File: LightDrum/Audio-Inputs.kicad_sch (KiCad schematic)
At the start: 18 parts, among them J4 XLR3, J5 SJ-43515RS-SMT-TR, K3 2-SW-RELAY, U41 SSM3K361R_SOT23F, U7 OPA1652

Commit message: Add docs and gerbers for REV7
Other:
- title: Audio Inputs -> LightDrum
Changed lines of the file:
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@@
   (paper "A4")
   (title_block
-    (title "Audio Inputs")
-    (rev "REV6")
+    (title "LightDrum")
+    (rev "REV7")
     (company "Daxxn Industries")
   )

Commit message: First pass over schematic (WIP)
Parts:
- removed K3: 2-SW-RELAY, Daxxn_Relays:AGQ200S4HZ, symbol Daxxn_Relays:2-SW-RELAY
- removed R100, R99: ${DIFF-RES}, Resistor_SMD:R_0805_2012Metric, symbol Device:R_Small_US
- removed R101: 470${RES}, Resistor_SMD:R_0805_2012Metric, symbol Device:R_Small_US
- removed R102: 100${RES}, Resistor_SMD:R_0805_2012Metric, symbol Device:R_Small_US
- removed R103: ${P-RES}, Resistor_SMD:R_0805_2012Metric, symbol Device:R_Small_US
- removed U41: SSM3K361R_SOT23F, Package_TO_SOT_SMD:SOT-23, symbol Daxxn_Transistors:SSM3K361R_SOT23F
- removed U7: OPA1652, Package_SO:VSSOP-8_3.0x3.0mm_P0.65mm, symbol Daxxn_OPAMP:OPA1652
- added C12, C16: 100nF, Capacitor_SMD:C_0603_1608Metric, symbol Device:C_Small
- added C13, C14, C17, C18: 10uF, Capacitor_SMD:C_1210_3225Metric, symbol Device:C_Small
- added C15, C19: 4.7uF, Capacitor_SMD:C_0805_2012Metric, symbol Device:C_Small
- added R10, R11: 330, Resistor_SMD:R_0805_2012Metric, symbol Device:R_Small_US
- added R4, R7: 14.67K, Resistor_SMD:R_0603_1608Metric, symbol Device:R_Small_US
- added R5, R8: 10K, Resistor_SMD:R_0603_1608Metric, symbol Device:R_Small_US
- added R6, R9: 100K, Resistor_SMD:R_0603_1608Metric, symbol Device:R_Small_US
- added RV1, RV2: 30K, Potentiometer_SMD:Potentiometer_Bourns_TC33X_Vertical, symbol Device:R_Potentiometer_Small
- added U-HP-VREF1, U-XLR-VREF1: TPS7A94, Daxxn_Packages:WSON-10-1EP_3x3mm, symbol Daxxn_Regulators:TPS7A94
- added U-HP1, U-XLR1: MCP3550-60-ESN, symbol Analog_ADC:MCP3550-60-ESN
- D8: value HP IND - RED -> HP IND - BLUE
- D9: value XLR IND - RED -> XLR IND - BLUE
- R92, R97, R98: value 100${RES} -> 100
- R93: value ${P-RES} -> 10K
- R95, R96: value ${DIFF-RES} -> 100
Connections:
- net GND: now also J4.1, C12.2, C13.2, C14.2, C15.2, C16.2, C17.2, C18.2, C19.2, R6.2, R9.2, RV1.2, RV1.3, RV2.2, RV2.3, U-HP-VREF1.11 (GND), U-HP-VREF1.6 (GND), U-HP1.4 (VSS), U-XLR-VREF1.11 (GND), U-XLR-VREF1.6 (GND), U-XLR1.4 (VSS)
- net at R97.2, R98.2: now also U-HP1.2 (Vin+)
- net at R96.2: now also U-XLR1.3 (Vin-)
- net at R95.2: now also U-XLR1.2 (Vin+)
- net at D9.2 (A): now also R11.2
- net at D8.2 (A): now also R10.2
- net GNDA: no longer names the net of J5.S
- net GNDA: now also U-HP1.3 (Vin-); no longer J4.1
- new net: R5.2, U-XLR-VREF1.3 (EN_UV)
- new net: R4.2, R6.1, U-XLR-VREF1.5 (FB_PG)
- new net: C15.1, RV1.1, U-XLR-VREF1.7 (NR/SS)
- new net: R7.2, R9.1, U-HP-VREF1.5 (FB_PG)
- new net: R8.2, U-HP-VREF1.3 (EN_UV)
- new net: C19.1, RV2.1, U-HP-VREF1.7 (NR/SS)
- new net HP-ADC-CS: U-HP1.7 (~{CS})
- new net HP-SEL-IND: R10.1
- new net HP-VREF: C17.1, R7.1, U-HP-VREF1.10 (OUT), U-HP-VREF1.8 (SNS), U-HP-VREF1.9 (OUT), U-HP1.1 (Vref)
- new net HP-VREF-PG: U-HP-VREF1.4 (PG)
- new net SPI-COPI: U-HP1.6 (SDO/~{RDY}), U-XLR1.6 (SDO/~{RDY})
- new net SPI-SCLK: U-HP1.5 (SCK), U-XLR1.5 (SCK)
- new net VDD: C12.1, C14.1, C16.1, C18.1, R5.1, R8.1, U-HP-VREF1.1 (IN), U-HP-VREF1.2 (IN), U-HP1.8 (VDD), U-XLR-VREF1.1 (IN), U-XLR-VREF1.2 (IN), U-XLR1.8 (VDD)
- new net XLR-ADC-CS: U-XLR1.7 (~{CS})
- new net XLR-SEL-IND: R11.1
- new net XLR-VREF: C13.1, R4.1, U-XLR-VREF1.10 (OUT), U-XLR-VREF1.8 (SNS), U-XLR-VREF1.9 (OUT), U-XLR1.1 (Vref)
- new net XLR-VREF-PG: U-XLR-VREF1.4 (PG)
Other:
- note added: "AUDIO ADCS"
- note added: "Extra adjustable regulation on the ADCs VREF lines."
- note added: "THIS IS OVERKILL AS FUCK. I LIKE IT."
- note added: "The HP-SWITCH sends a signal to the MC, setting the HP jack as a possible audio source."
- note removed: "AUDIO SOURCE SELECTION"
- moved on the sheet: D8, D9, J4, J5, R92, R93, R95, R96, R97, R98

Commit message: Clean up and remove old files
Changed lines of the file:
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@@
     (stroke (width 0) (type default) (color 0 0 0 0))
   )
-  (wire (pts (xy 134.62 38.1) (xy 138.43 38.1))
+  (wire (pts (xy 123.19 38.1) (xy 138.43 38.1))
     (stroke (width 0) (type default) (color 0 0 0 0))
   )
@@
     (effects (font (size 1.27 1.27)) (justify left bottom))
   )
+  (label "XLR-VREF" (at 123.19 38.1 0)
+    (effects (font (size 1.27 1.27)) (justify left bottom))
+  )
   (label "XLR-VREF" (at 69.85 63.5 0)
     (effects (font (size 1.27 1.27)) (justify left bottom))
@@
     (effects (font (size 1.27 1.27)) (justify right))
   )
-  (hierarchical_label "XLR-VREF" (shape output) (at 134.62 38.1 180)
-    (effects (font (size 1.27 1.27)) (justify right))
-  )

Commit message: General component placement
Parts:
- removed U-HP1, U-XLR1: MCP3550-60-ESN, symbol Analog_ADC:MCP3550-60-ESN
- added U-HP201, U-XLR201: MCP3553-ESN, Package_SO:MSOP-8_3x3mm_P0.65mm, symbol Analog_ADC:MCP3553-ESN
- J202: renamed from J5; PartNumber (none) -> 0407-0001
- R202: renamed from R5; footprint Resistor_SMD:R_0603_1608Metric -> Resistor_SMD:R_0402_1005Metric
- R208: renamed from R8; footprint Resistor_SMD:R_0603_1608Metric -> Resistor_SMD:R_0402_1005Metric
- RV201: renamed from RV1; footprint Potentiometer_SMD:Potentiometer_Bourns_TC33X_Vertical -> Daxxn_Switches:Bourns_TC33X
- RV202: renamed from RV2; footprint Potentiometer_SMD:Potentiometer_Bourns_TC33X_Vertical -> Daxxn_Switches:Bourns_TC33X
- renumbered C12 to C201, C13 to C202, C14 to C203, C15 to C204, C16 to C205, C17 to C206, C18 to C207, C19 to C208, D8 to D201, D9 to D202, J4 to J201, R4 to R201, R95 to R203, R96 to R204, R6 to R205, R97 to R206, R7 to R207, R98 to R209, R9 to R210, R92 to R211, R93 to R212, R10 to R213, R11 to R214, U-HP-VREF1 to U-HP-VREF201, U-XLR-VREF1 to U-XLR-VREF201
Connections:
- net GND: now also U-HP201.4 (VSS), U-XLR201.4 (VSS)
- net HP-ADC-CS: now also U-HP201.7 (~{CS})
- net HP-VREF: now also U-HP201.1 (Vref)
- net SPI-COPI: now also U-HP201.6 (SDO/~{RDY}), U-XLR201.6 (SDO/~{RDY})
- net SPI-SCLK: now also U-HP201.5 (SCK), U-XLR201.5 (SCK)
- net VDD: now also U-HP201.8 (VDD), U-XLR201.8 (VDD)
- net XLR-ADC-CS: now also U-XLR201.7 (~{CS})
- net XLR-VREF: now also U-XLR201.1 (Vref)
- net HP+: now reaches R206.2, R209.2
- net HP+: now also U-HP201.2 (Vin+)
- net XLR-: now reaches R204.2
- net XLR-: now also U-XLR201.3 (Vin-)
- net XLR+: now reaches R203.2
- net XLR+: now also U-XLR201.2 (Vin+)
- net HP-: now reaches J202.S
- net HP-: now also U-HP201.3 (Vin-)

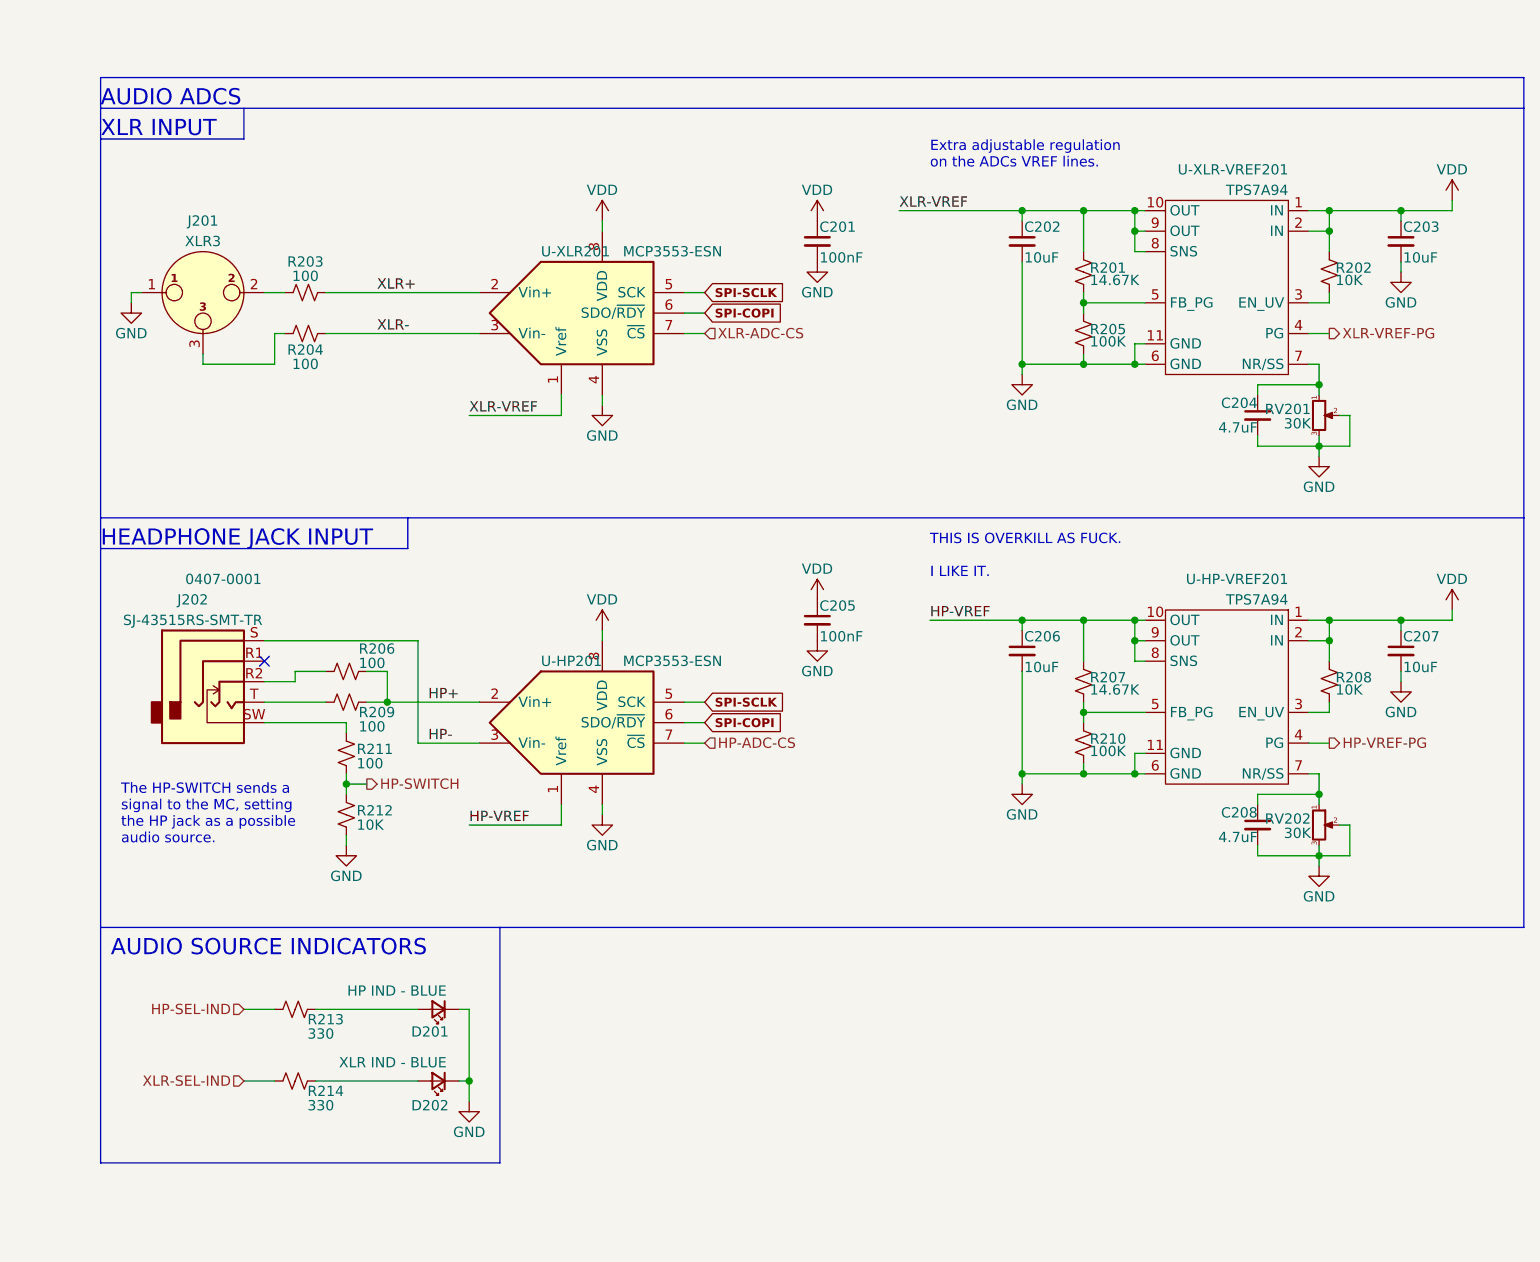
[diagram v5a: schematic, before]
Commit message: Simplify analog power supply and add some routing
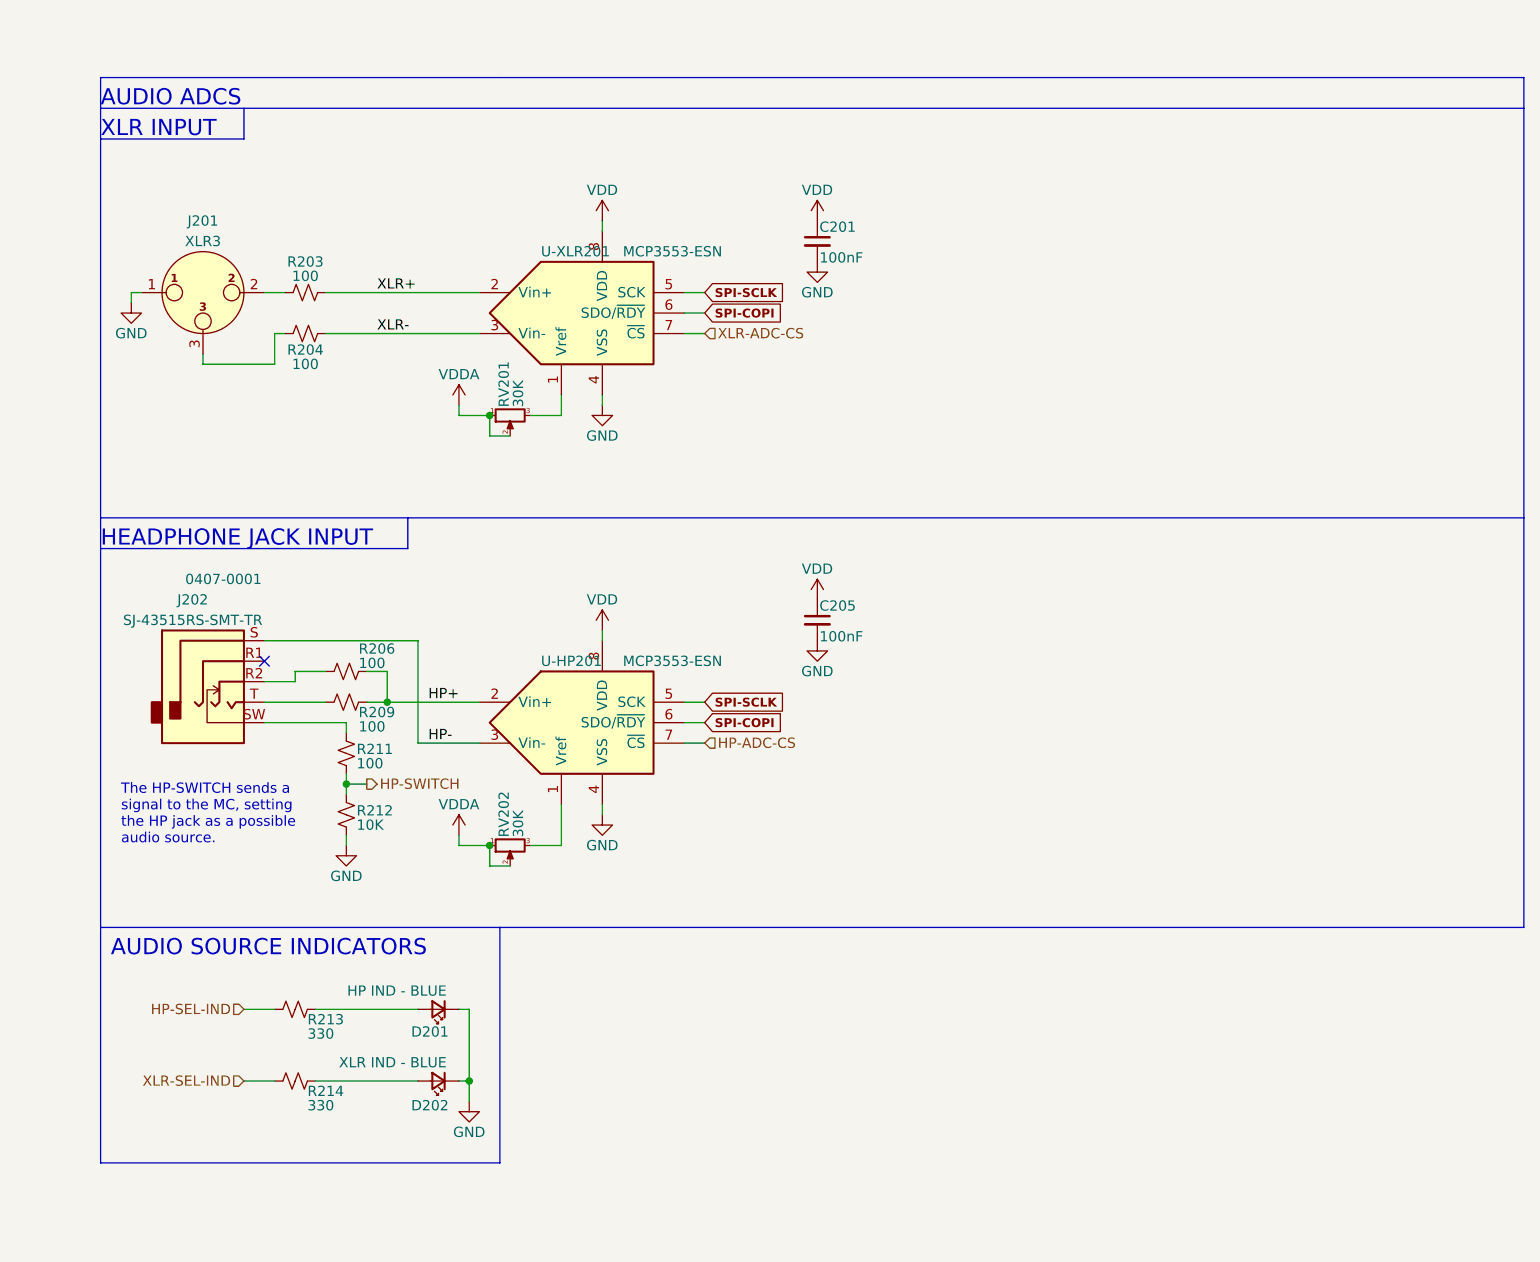
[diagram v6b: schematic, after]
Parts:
- removed C202, C203, C206, C207: 10uF, Capacitor_SMD:C_1210_3225Metric, symbol Device:C_Small
- removed C204, C208: 4.7uF, Capacitor_SMD:C_0805_2012Metric, symbol Device:C_Small
- removed R201, R207: 14.67K, Resistor_SMD:R_0603_1608Metric, symbol Device:R_Small_US
- removed R202, R208: 10K, Resistor_SMD:R_0402_1005Metric, symbol Device:R_Small_US
- removed R205, R210: 100K, Resistor_SMD:R_0603_1608Metric, symbol Device:R_Small_US
- removed U-HP-VREF201, U-XLR-VREF201: TPS7A94, Daxxn_Packages:WSON-10-1EP_3x3mm, symbol Daxxn_Regulators:TPS7A94
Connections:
- net GND: no longer RV201.2, RV201.3, RV202.2, RV202.3
- net VDDA: now reaches RV201.1
- net VDDA: now also RV201.2, RV202.1, RV202.2
- net HP-VREF: no longer names the net of U-HP201.1 (Vref)
- net HP-VREF: now also RV202.3
- net XLR-VREF: no longer names the net of U-XLR201.1 (Vref)
- net XLR-VREF: now also RV201.3
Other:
- note removed: "Extra adjustable regulation on the ADCs VREF lines."
- note removed: "THIS IS OVERKILL AS FUCK. I LIKE IT."

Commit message: Replace barrel jacks with proper DIN4 conn and more
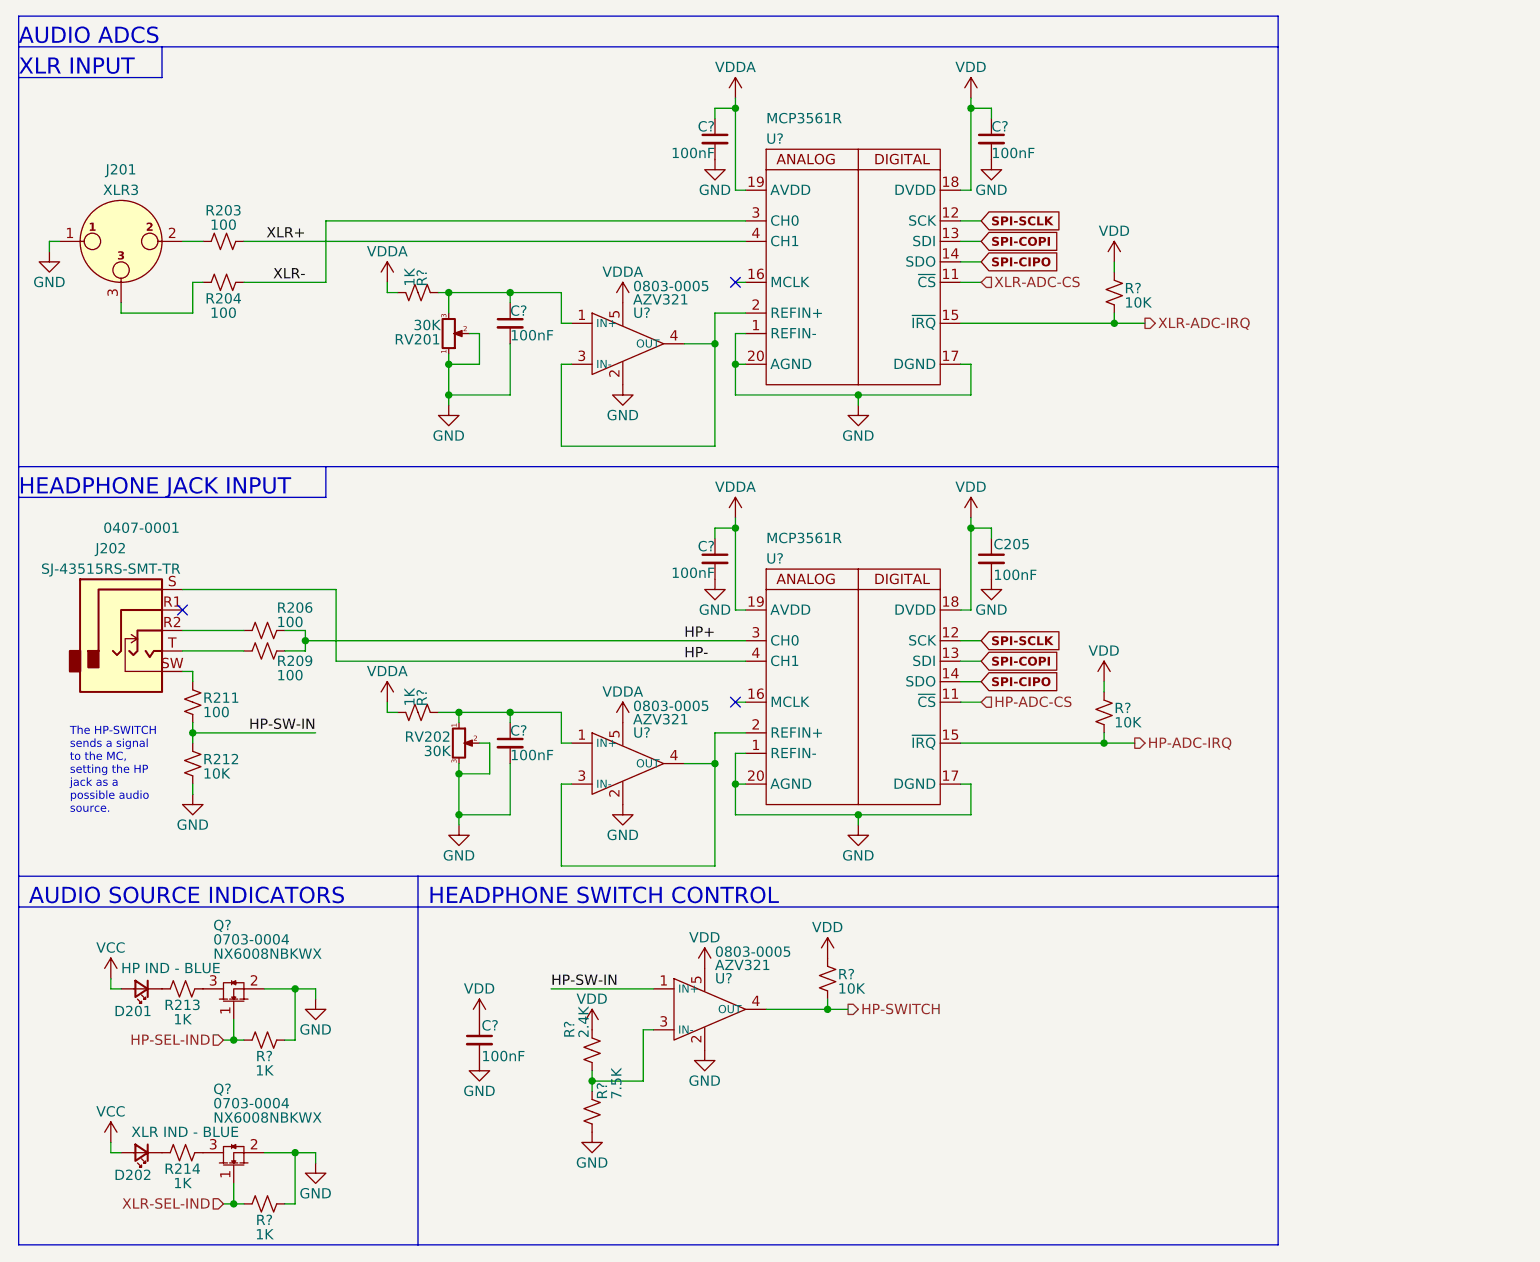
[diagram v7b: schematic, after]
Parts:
- removed C201: 100nF, Capacitor_SMD:C_0603_1608Metric, symbol Device:C_Small
- removed U-HP201, U-XLR201: MCP3553-ESN, Package_SO:MSOP-8_3x3mm_P0.65mm, symbol Analog_ADC:MCP3553-ESN
- added C? (x6): 100nF, Capacitor_SMD:C_0603_1608Metric, symbol Device:C_Small
- added Q? (x2): NX6008NBKWX, Package_TO_SOT_SMD:SOT-323_SC-70, symbol Daxxn_Transistors:NX6008NBKWX
- added R? (x2): 1K, Resistor_SMD:R_0603_1608Metric, symbol Device:R_Small_US
- added R? (x3): 10K, Resistor_SMD:R_0805_2012Metric, symbol Device:R_Small_US
- added R?: 2.4K, Resistor_SMD:R_0805_2012Metric, symbol Device:R_Small_US
- added R? (x2): 1K, Resistor_SMD:R_0805_2012Metric, symbol Device:R_Small_US
- added R?: 7.5K, Resistor_SMD:R_0805_2012Metric, symbol Device:R_Small_US
- added U? (x3): AZV321, Package_TO_SOT_SMD:SOT-23-5, symbol Daxxn_OPAMP:AZV321
- added U? (x2): MCP3561R, Package_DFN_QFN:QFN-20-1EP_3x3mm_P0.4mm_EP1.65x1.65mm, symbol Daxxn_IC:MCP3561R
- D201: SupplierPN (none) -> LTST-S321TBKT
- R213, R214: value 330 -> 1K
- RV201, RV202: footprint Daxxn_Switches:Bourns_TC33X -> Potentiometer_SMD:Potentiometer_Bourns_3214W_Vertical
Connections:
- net HP+: now also U?.3 (CH0)
- net HP-: now also U?.4 (CH1)
- net HP-ADC-CS: now also U?.11 (~{CS})
- net HP-SEL-IND: now also Q?.1 (G), R?.2; no longer R213.1
- net HP-SWITCH: now also R?.1, U?.4 (OUT); no longer R211.1, R212.2
- net SPI-COPI: now also U?.13 (SDI), U?.13 (SDI)
- net SPI-SCLK: now also U?.12 (SCK), U?.12 (SCK)
- net VDD: now also C?.1, C?.1, R?.2, R?.2, R?.2, R?.2, U?.18 (DVDD), U?.18 (DVDD), U?.5 (V+)
- net VDDA: now also C?.1, C?.1, R?.2, R?.2, U?.19 (AVDD), U?.19 (AVDD), U?.5 (V+), U?.5 (V+); no longer RV201.1, RV201.2, RV202.1, RV202.2
- net XLR+: now also U?.4 (CH1)
- net XLR-: now also U?.3 (CH0)
- net XLR-ADC-CS: now also U?.11 (~{CS})
- net XLR-SEL-IND: now also Q?.1 (G), R?.2; no longer R214.1
- net at R214.2: now also D202.1 (K); no longer D202.2 (A)
- net at RV201.3: now also C?.1, R?.1, U?.1 (IN+)
- net at R213.2: now also D201.1 (K); no longer D201.2 (A)
- net AGND: now reaches RV202.3
- net AGND: now also C205.2, J201.1, R212.1, RV201.1, RV201.2, RV202.2, C?.2, C?.2, C?.2, C?.2, C?.2, C?.2, Q?.2 (S), Q?.2 (S), R?.1, R?.1, R?.1, U?.1 (REFIN-), U?.1 (REFIN-), U?.10 (NC), U?.10 (NC), U?.17 (DGND), U?.17 (DGND), U?.2 (V-), U?.2 (V-), U?.2 (V-), U?.20 (AGND), U?.20 (AGND), U?.21 (AGND), U?.21 (AGND), U?.5 (NC), U?.5 (NC), U?.6 (NC), U?.6 (NC), U?.7 (NC), U?.7 (NC), U?.8 (NC), U?.8 (NC), U?.9 (NC), U?.9 (NC)
- removed net GND: C205.2, D201.1 (K), D202.1 (K), J201.1, R212.1
- new net: Q?.3 (D), R214.1
- new net: C?.1, R?.1, RV202.1, U?.1 (IN+)
- new net: U?.2 (REFIN+), U?.3 (IN-), U?.4 (OUT) (x2)
- new net: Q?.3 (D), R213.1
- new net: R?.1, R?.2, U?.3 (IN-)
- new net HP-ADC-IRQ: R?.1, U?.15 (~{IRQ})
- new net HP-SW-IN: R211.1, R212.2, U?.1 (IN+)
- new net SPI-CIPO: U?.14 (SDO), U?.14 (SDO)
- new net VCC: D201.2 (A), D202.2 (A)
- new net XLR-ADC-IRQ: R?.1, U?.15 (~{IRQ})
- no-connect marks 1 -> 3
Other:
- note added: "HEADPHONE SWITCH CONTROL"
- moved on the sheet: C205, D201, D202, J201, J202, R203, R204, R206, R209, R211, R212, R213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
